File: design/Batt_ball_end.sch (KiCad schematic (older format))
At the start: 6 parts

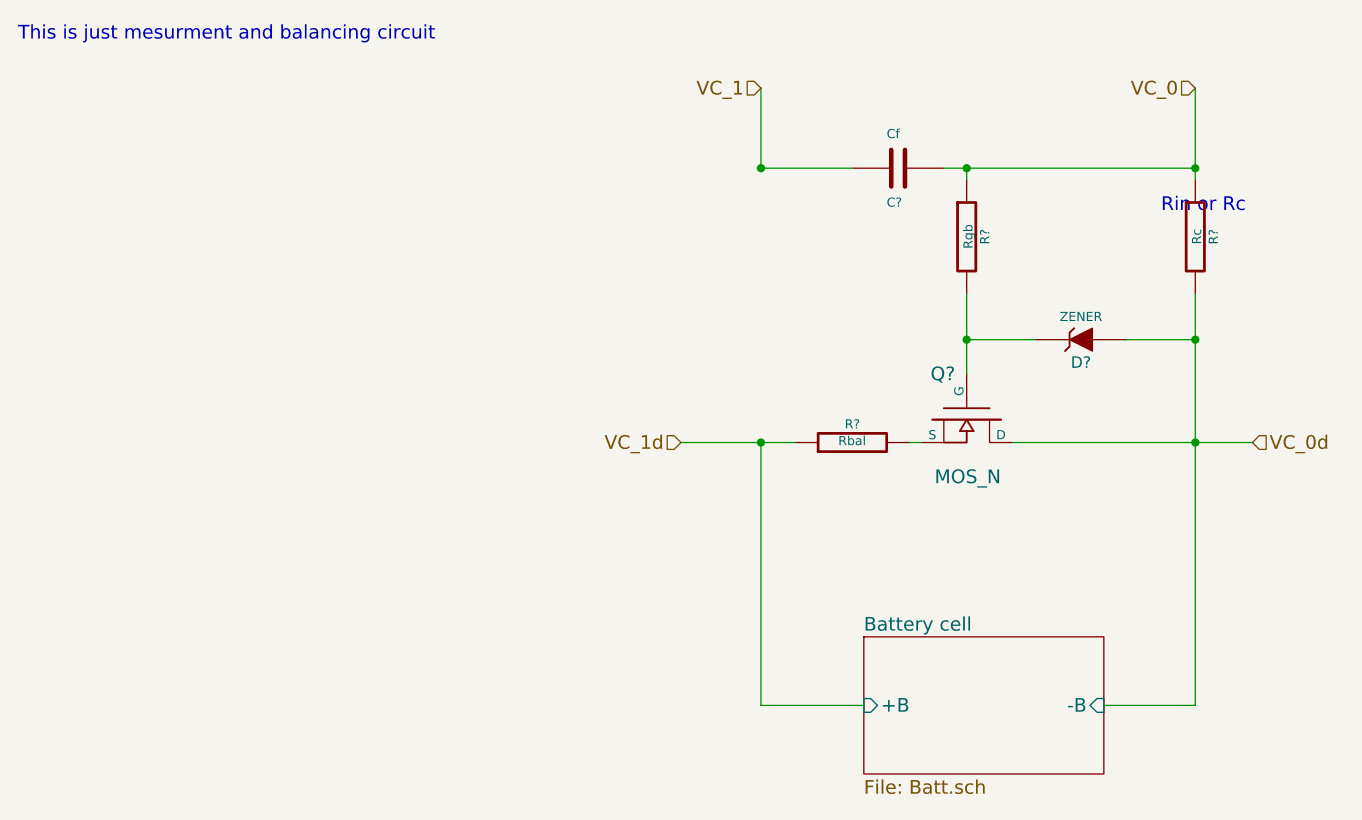
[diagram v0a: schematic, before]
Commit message: Add a cell to 10 but currently a scheme is a total mess fix it
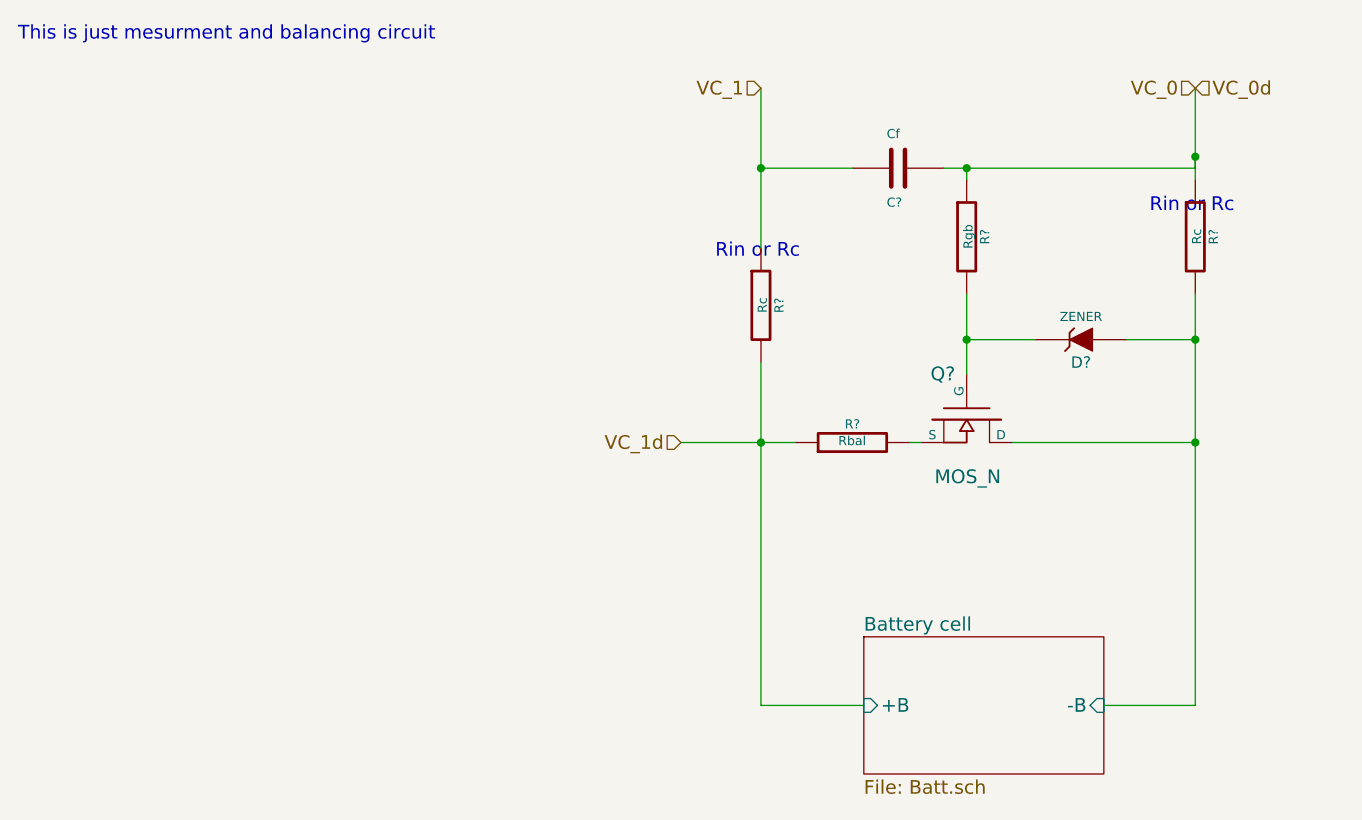
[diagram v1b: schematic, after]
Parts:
- added R?: Rc, symbol R
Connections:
- net VC_1: now also R?.1
- net VC_1d: now also R?.2
- net VC_0d renamed Battery cell/-B
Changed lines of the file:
@@
 $Descr A4 11693 8268
 encoding utf-8
-Sheet 23 30
+Sheet 15 30
 Title ""
 Date ""
@@
 U 1 1 55BD57AA
 P 5400 2750
-AR Path="/55BB8FBC/3A501D31/55BD57AA" Ref="Q?"  Part="1"
-AR Path="/55BB8FBC/3A507C61/55BD57AA" Ref="Q?"  Part="1"
-AR Path="/55BB8FBC/3A509CE9/55BD57AA" Ref="Q?"  Part="1"
-AR Path="/55BB8FBC/3A53CBC8/55BD57AA" Ref="Q?"  Part="1"
+AR Path="/55BB8FBC/3A50D488/55BD57AA" Ref="Q?"  Part="1"
+AR Path="/55BB8FBC/3A51DCAC/55BD57AA" Ref="Q?"  Part="1"
+AR Path="/55BB8FBC/3A50984C/55BD57AA" Ref="Q?"  Part="1"
 F 0 "Q?" V 5200 2700 60  0000 R CNN
 F 1 "MOS_N" V 5650 2900 60  0000 R CNN
@@
 U 1 1 55BD5928
 P 4900 2850
-AR Path="/55BB8FBC/3A501D31/55BD5928" Ref="R?"  Part="1"
-AR Path="/55BB8FBC/3A507C61/55BD5928" Ref="R?"  Part="1"
-AR Path="/55BB8FBC/3A509CE9/55BD5928" Ref="R?"  Part="1"
-AR Path="/55BB8FBC/3A53CBC8/55BD5928" Ref="R?"  Part="1"
+AR Path="/55BB8FBC/3A50D488/55BD5928" Ref="R?"  Part="1"
+AR Path="/55BB8FBC/3A51DCAC/55BD5928" Ref="R?"  Part="1"
+AR Path="/55BB8FBC/3A50984C/55BD5928" Ref="R?"  Part="1"
 F 0 "R?" V 4980 2850 40  0000 C CNN
 F 1 "Rbal" V 4907 2851 40  0000 C CNN
@@
 U 1 1 55BD5ABC
 P 5900 2400
-AR Path="/55BB8FBC/3A501D31/55BD5ABC" Ref="D?"  Part="1"
-AR Path="/55BB8FBC/3A507C61/55BD5ABC" Ref="D?"  Part="1"
-AR Path="/55BB8FBC/3A509CE9/55BD5ABC" Ref="D?"  Part="1"
-AR Path="/55BB8FBC/3A53CBC8/55BD5ABC" Ref="D?"  Part="1"
+AR Path="/55BB8FBC/3A50D488/55BD5ABC" Ref="D?"  Part="1"
+AR Path="/55BB8FBC/3A51DCAC/55BD5ABC" Ref="D?"  Part="1"
+AR Path="/55BB8FBC/3A50984C/55BD5ABC" Ref="D?"  Part="1"
 F 0 "D?" H 5900 2500 50  0000 C CNN
 F 1 "ZENER" H 5900 2300 40  0000 C CNN
@@
 U 1 1 55BD5B30
 P 6400 1950
-AR Path="/55BB8FBC/3A501D31/55BD5B30" Ref="R?"  Part="1"
-AR Path="/55BB8FBC/3A507C61/55BD5B30" Ref="R?"  Part="1"
-AR Path="/55BB8FBC/3A509CE9/55BD5B30" Ref="R?"  Part="1"
-AR Path="/55BB8FBC/3A53CBC8/55BD5B30" Ref="R?"  Part="1"
+AR Path="/55BB8FBC/3A50D488/55BD5B30" Ref="R?"  Part="1"
+AR Path="/55BB8FBC/3A51DCAC/55BD5B30" Ref="R?"  Part="1"
+AR Path="/55BB8FBC/3A50984C/55BD5B30" Ref="R?"  Part="1"
 F 0 "R?" V 6480 1950 40  0000 C CNN
 F 1 "Rc" V 6407 1951 40  0000 C CNN
@@
 $EndComp
 $Comp
+L R R?
+U 1 1 55BD5E1E
+P 4500 2250
+AR Path="/55BB8FBC/3A50D488/55BD5E1E" Ref="R?"  Part="1"
+AR Path="/55BB8FBC/3A51DCAC/55BD5E1E" Ref="R?"  Part="1"
+AR Path="/55BB8FBC/3A50984C/55BD5E1E" Ref="R?"  Part="1"
+F 0 "R?" V 4580 2250 40  0000 C CNN
+F 1 "Rc" V 4507 2251 40  0000 C CNN
+F 2 "" V 4430 2250 30  0000 C CNN
+F 3 "" H 4500 2250 30  0000 C CNN
+	1    4500 2250
+	1    0    0    -1
+$EndComp
+$Comp
 L C C?
 U 1 1 55BD5F3E
 P 5100 1650
-AR Path="/55BB8FBC/3A501D31/55BD5F3E" Ref="C?"  Part="1"
-AR Path="/55BB8FBC/3A507C61/55BD5F3E" Ref="C?"  Part="1"
-AR Path="/55BB8FBC/3A509CE9/55BD5F3E" Ref="C?"  Part="1"
-AR Path="/55BB8FBC/3A53CBC8/55BD5F3E" Ref="C?"  Part="1"
+AR Path="/55BB8FBC/3A50D488/55BD5F3E" Ref="C?"  Part="1"
+AR Path="/55BB8FBC/3A51DCAC/55BD5F3E" Ref="C?"  Part="1"
+AR Path="/55BB8FBC/3A50984C/55BD5F3E" Ref="C?"  Part="1"
 F 0 "C?" V 5250 1600 40  0000 L CNN
 F 1 "Cf" V 4950 1600 40  0000 L CNN
@@
 	0    1    1    0
 $EndComp
+$Comp
+L R R?
+U 1 1 55BD60D7
+P 5400 1950
+AR Path="/55BB8FBC/3A50D488/55BD60D7" Ref="R?"  Part="1"
+AR Path="/55BB8FBC/3A51DCAC/55BD60D7" Ref="R?"  Part="1"
+AR Path="/55BB8FBC/3A50984C/55BD60D7" Ref="R?"  Part="1"
+F 0 "R?" V 5480 1950 40  0000 C CNN
+F 1 "Rgb" V 5407 1951 40  0000 C CNN
+F 2 "" V 5330 1950 30  0000 C CNN
+F 3 "" H 5400 1950 30  0000 C CNN
+	1    5400 1950
+	1    0    0    -1
+$EndComp
+Text HLabel 4500 1300 0    60   Input ~ 0
+VC_1
+Text HLabel 6400 1300 0    60   Input ~ 0
+VC_0
+Text HLabel 4150 2850 0    60   Input ~ 0
+VC_1d
+Text HLabel 6400 1300 2    60   Input ~ 0
+VC_0d
+Text Notes 6200 1850 0    60   ~ 0
+Rin or Rc
+Wire Wire Line
+	4500 1300 4500 2000
 Connection ~ 4500 2850
 Wire Wire Line
 	4150 2850 4650 2850
-Wire Wire Line
-	4500 4000 4950 4000
 Wire Wire Line
 	5150 2850 5200 2850
@@
 	6400 4000 6000 4000
 Wire Wire Line
-	5600 2850 6650 2850
-Wire Wire Line
-	5300 1650 6400 1650
-Wire Wire Line
 	6400 1300 6400 1700
 Wire Wire Line
 	4500 1650 4900 1650
-$Comp
-L R R?
-U 1 1 55BD60D7
-P 5400 1950
-AR Path="/55BB8FBC/3A501D31/55BD60D7" Ref="R?"  Part="1"
-AR Path="/55BB8FBC/3A507C61/55BD60D7" Ref="R?"  Part="1"
-AR Path="/55BB8FBC/3A509CE9/55BD60D7" Ref="R?"  Part="1"
-AR Path="/55BB8FBC/3A53CBC8/55BD60D7" Ref="R?"  Part="1"
-F 0 "R?" V 5480 1950 40  0000 C CNN
-F 1 "Rgb" V 5407 1951 40  0000 C CNN
-F 2 "" V 5330 1950 30  0000 C CNN
-F 3 "" H 5400 1950 30  0000 C CNN
-	1    5400 1950
-	1    0    0    -1
-$EndComp
 Wire Wire Line
 	5400 1700 5400 1650
@@
 Connection ~ 5400 2400
 Connection ~ 4500 1650
-Connection ~ 6400 1650
-Text HLabel 4500 1300 0    60   Input ~ 0
-VC_1
-Text HLabel 6400 1300 0    60   Input ~ 0
-VC_0
-Text HLabel 4150 2850 0    60   Input ~ 0
-VC_1d
-Text HLabel 6650 2850 2    60   Input ~ 0
-VC_0d
+Wire Wire Line
+	4500 2500 4500 4000
 Wire Wire Line
 	6400 4000 6400 2200
-Text Notes 6250 1850 0    60   ~ 0
+Wire Wire Line
+	5600 2850 6400 2850
+Text Notes 4300 2050 0    60   ~ 0
 Rin or Rc
 Wire Wire Line
-	4500 4000 4500 2850
+	5300 1650 6400 1650
 Wire Wire Line
-	4500 1650 4500 1300
+	6400 1650 6400 1600
+Connection ~ 6400 1600
+Wire Wire Line
+	4500 4000 4950 4000
 $EndSCHEMATC

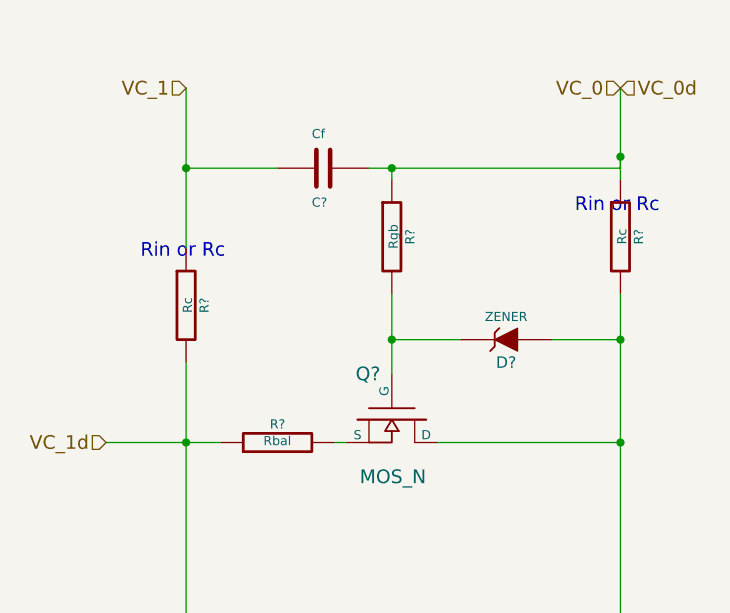
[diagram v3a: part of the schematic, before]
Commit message: Add new example in datasheet define more values
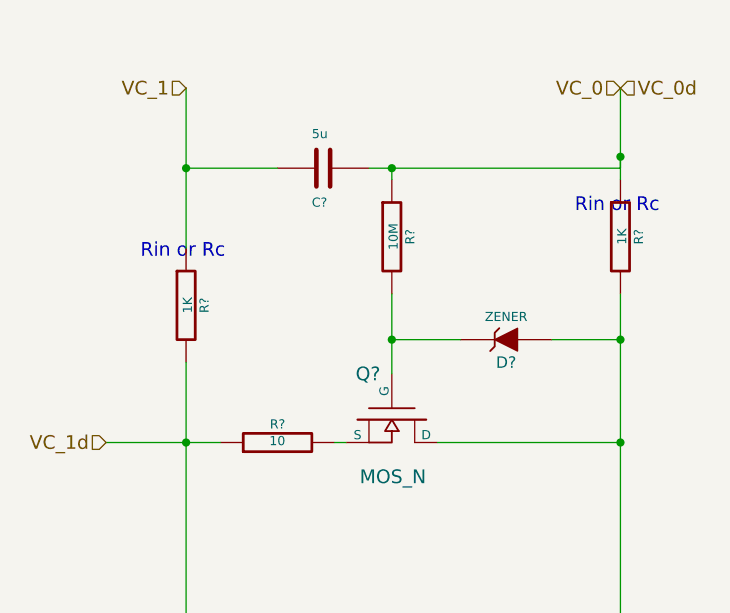
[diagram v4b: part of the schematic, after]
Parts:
- C?: value Cf -> 5u; Name (none) -> Cc
- R?: value Rbal -> 10
- R?: value Rc -> 1K; Name (none) -> Rc
- R?: value Rc -> 1K
- R?: value Rgb -> 10M
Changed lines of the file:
@@
 $Descr A4 11693 8268
 encoding utf-8
-Sheet 15 101
+Sheet 12 101
 Title ""
 Date ""
@@
 AR Path="/3A58CB36/3A54397C/55BD5928" Ref="R?"  Part="1"
 F 0 "R?" V 4980 2850 40  0000 C CNN
-F 1 "Rbal" V 4907 2851 40  0000 C CNN
+F 1 "10" V 4907 2851 40  0000 C CNN
 F 2 "" V 4830 2850 30  0000 C CNN
 F 3 "" H 4900 2850 30  0000 C CNN
@@
 AR Path="/3A58CB36/3A54397C/55BD5B30" Ref="R?"  Part="1"
 F 0 "R?" V 6480 1950 40  0000 C CNN
-F 1 "Rc" V 6407 1951 40  0000 C CNN
+F 1 "1K" V 6407 1951 40  0000 C CNN
 F 2 "" V 6330 1950 30  0000 C CNN
 F 3 "" H 6400 1950 30  0000 C CNN
+F 4 "Rc" V 6400 1950 60  0001 C CNN "Name"
 	1    6400 1950
 	1    0    0    -1
@@
 AR Path="/3A58CB36/3A54397C/55BD5E1E" Ref="R?"  Part="1"
 F 0 "R?" V 4580 2250 40  0000 C CNN
-F 1 "Rc" V 4507 2251 40  0000 C CNN
+F 1 "1K" V 4507 2251 40  0000 C CNN
 F 2 "" V 4430 2250 30  0000 C CNN
 F 3 "" H 4500 2250 30  0000 C CNN
@@
 AR Path="/3A58CB36/3A54397C/55BD5F3E" Ref="C?"  Part="1"
 F 0 "C?" V 5250 1600 40  0000 L CNN
-F 1 "Cf" V 4950 1600 40  0000 L CNN
+F 1 "5u" V 4950 1600 40  0000 L CNN
 F 2 "" H 5138 1500 30  0000 C CNN
 F 3 "" H 5100 1650 60  0000 C CNN
+F 4 "Cc" V 5100 1650 60  0001 C CNN "Name"
 	1    5100 1650
 	0    1    1    0
@@
 AR Path="/3A58CB36/3A54397C/55BD60D7" Ref="R?"  Part="1"
 F 0 "R?" V 5480 1950 40  0000 C CNN
-F 1 "Rgb" V 5407 1951 40  0000 C CNN
+F 1 "10M" V 5407 1951 40  0000 C CNN
 F 2 "" V 5330 1950 30  0000 C CNN
 F 3 "" H 5400 1950 30  0000 C CNN

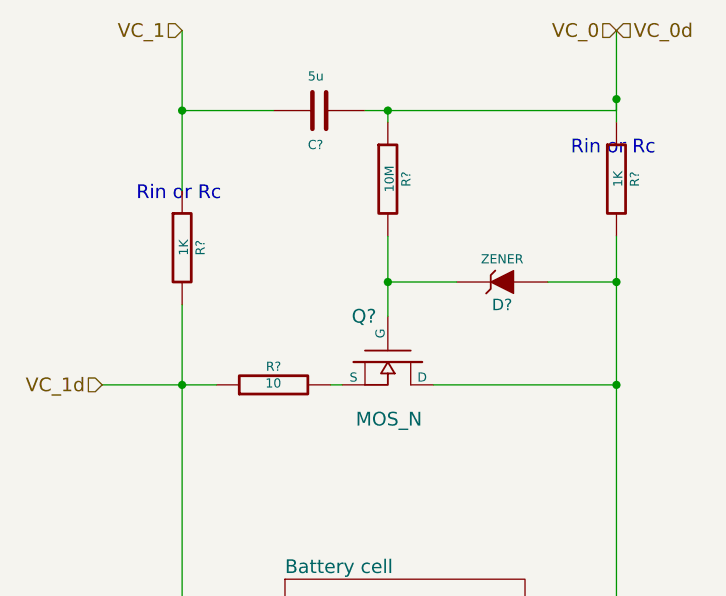
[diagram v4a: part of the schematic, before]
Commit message: Fix some schematic update pdf
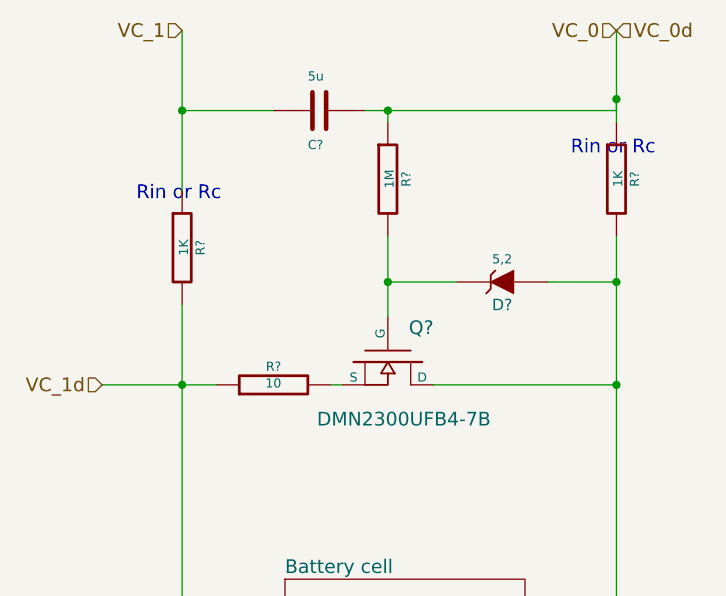
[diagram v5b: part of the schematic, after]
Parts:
- removed Q?: MOS_N, symbol MOS_N
- added Q?: DMN2300UFB4-7B, symbol MOSFET_N
- D?: value ZENER -> 5,2
- R?: value 10M -> 1M
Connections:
- net Battery cell/-B: now also Q?.D
- net at D?.2 (K), R?.2: now also Q?.G
- net at R?.2: now also Q?.S
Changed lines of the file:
@@
 This is just mesurment and balancing circuit
-$Comp
-L MOS_N Q?
-U 1 1 55BD57AA
-P 5400 2750
-AR Path="/55BB8FBC/3A50D488/55BD57AA" Ref="Q?"  Part="1"
-AR Path="/55BB8FBC/3A51DCAC/55BD57AA" Ref="Q?"  Part="1"
-AR Path="/55BB8FBC/3A50984C/55BD57AA" Ref="Q?"  Part="1"
-AR Path="/55BB8FBC/3A5B5476/3A50984C/55BD57AA" Ref="Q?"  Part="1"
-AR Path="/55BB8FBC/3A5B5476/3A54231A/55BD57AA" Ref="Q?"  Part="1"
-AR Path="/55BB8FBC/3A5B5476/3A54397C/55BD57AA" Ref="Q?"  Part="1"
-AR Path="/3A58CB36/3A50984C/55BD57AA" Ref="Q?"  Part="1"
-AR Path="/3A58CB36/3A54231A/55BD57AA" Ref="Q?"  Part="1"
-AR Path="/3A58CB36/3A54397C/55BD57AA" Ref="Q?"  Part="1"
-F 0 "Q?" V 5200 2700 60  0000 R CNN
-F 1 "MOS_N" V 5650 2900 60  0000 R CNN
-F 2 "" H 5400 2750 60  0000 C CNN
-F 3 "" H 5400 2750 60  0000 C CNN
-	1    5400 2750
-	0    1    1    0
-$EndComp
 $Comp
 L R R?
@@
 AR Path="/3A58CB36/3A54231A/55BD5928" Ref="R?"  Part="1"
 AR Path="/3A58CB36/3A54397C/55BD5928" Ref="R?"  Part="1"
+AR Path="/55C14E4B/3A5B5476/3A50984C/55BD5928" Ref="R?"  Part="1"
+AR Path="/55C14E4B/3A5B5476/3A54231A/55BD5928" Ref="R?"  Part="1"
+AR Path="/55C14E4B/3A5B5476/3A54397C/55BD5928" Ref="R?"  Part="1"
 F 0 "R?" V 4980 2850 40  0000 C CNN
 F 1 "10" V 4907 2851 40  0000 C CNN
@@
 AR Path="/3A58CB36/3A54231A/55BD5ABC" Ref="D?"  Part="1"
 AR Path="/3A58CB36/3A54397C/55BD5ABC" Ref="D?"  Part="1"
+AR Path="/55C14E4B/3A5B5476/3A50984C/55BD5ABC" Ref="D?"  Part="1"
+AR Path="/55C14E4B/3A5B5476/3A54231A/55BD5ABC" Ref="D?"  Part="1"
+AR Path="/55C14E4B/3A5B5476/3A54397C/55BD5ABC" Ref="D?"  Part="1"
 F 0 "D?" H 5900 2500 50  0000 C CNN
-F 1 "ZENER" H 5900 2300 40  0000 C CNN
+F 1 "5,2" H 5900 2300 40  0000 C CNN
 F 2 "" H 5900 2400 60  0000 C CNN
 F 3 "" H 5900 2400 60  0000 C CNN
@@
 AR Path="/3A58CB36/3A54231A/55BD5B30" Ref="R?"  Part="1"
 AR Path="/3A58CB36/3A54397C/55BD5B30" Ref="R?"  Part="1"
+AR Path="/55C14E4B/3A5B5476/3A50984C/55BD5B30" Ref="R?"  Part="1"
+AR Path="/55C14E4B/3A5B5476/3A54231A/55BD5B30" Ref="R?"  Part="1"
+AR Path="/55C14E4B/3A5B5476/3A54397C/55BD5B30" Ref="R?"  Part="1"
 F 0 "R?" V 6480 1950 40  0000 C CNN
 F 1 "1K" V 6407 1951 40  0000 C CNN
@@
 AR Path="/3A58CB36/3A54231A/55BD5E1E" Ref="R?"  Part="1"
 AR Path="/3A58CB36/3A54397C/55BD5E1E" Ref="R?"  Part="1"
+AR Path="/55C14E4B/3A5B5476/3A50984C/55BD5E1E" Ref="R?"  Part="1"
+AR Path="/55C14E4B/3A5B5476/3A54231A/55BD5E1E" Ref="R?"  Part="1"
+AR Path="/55C14E4B/3A5B5476/3A54397C/55BD5E1E" Ref="R?"  Part="1"
 F 0 "R?" V 4580 2250 40  0000 C CNN
 F 1 "1K" V 4507 2251 40  0000 C CNN
@@
 AR Path="/3A58CB36/3A54231A/55BD5F3E" Ref="C?"  Part="1"
 AR Path="/3A58CB36/3A54397C/55BD5F3E" Ref="C?"  Part="1"
+AR Path="/55C14E4B/3A5B5476/3A50984C/55BD5F3E" Ref="C?"  Part="1"
+AR Path="/55C14E4B/3A5B5476/3A54231A/55BD5F3E" Ref="C?"  Part="1"
+AR Path="/55C14E4B/3A5B5476/3A54397C/55BD5F3E" Ref="C?"  Part="1"
 F 0 "C?" V 5250 1600 40  0000 L CNN
 F 1 "5u" V 4950 1600 40  0000 L CNN
@@
 AR Path="/3A58CB36/3A54231A/55BD60D7" Ref="R?"  Part="1"
 AR Path="/3A58CB36/3A54397C/55BD60D7" Ref="R?"  Part="1"
+AR Path="/55C14E4B/3A5B5476/3A50984C/55BD60D7" Ref="R?"  Part="1"
+AR Path="/55C14E4B/3A5B5476/3A54231A/55BD60D7" Ref="R?"  Part="1"
+AR Path="/55C14E4B/3A5B5476/3A54397C/55BD60D7" Ref="R?"  Part="1"
 F 0 "R?" V 5480 1950 40  0000 C CNN
-F 1 "10M" V 5407 1951 40  0000 C CNN
+F 1 "1M" V 5407 1951 40  0000 C CNN
 F 2 "" V 5330 1950 30  0000 C CNN
 F 3 "" H 5400 1950 30  0000 C CNN
@@
 Wire Wire Line
 	4500 4000 4950 4000
+$Comp
+L MOSFET_N Q?
+U 1 1 55DFB94F
+P 5400 2750
+AR Path="/55BB8FBC/3A5B5476/3A54231A/55DFB94F" Ref="Q?"  Part="1"
+AR Path="/55BB8FBC/3A5B5476/3A54397C/55DFB94F" Ref="Q?"  Part="1"
+AR Path="/55BB8FBC/3A5B5476/3A50984C/55DFB94F" Ref="Q?"  Part="1"
+F 0 "Q?" V 5250 2950 60  0000 R CNN
+F 1 "DMN2300UFB4-7B" V 5650 3200 60  0000 R CNN
+F 2 "" H 5400 2750 60  0000 C CNN
+F 3 "" H 5400 2750 60  0000 C CNN
+	1    5400 2750
+	0    1    1    0
+$EndComp
 $EndSCHEMATC
